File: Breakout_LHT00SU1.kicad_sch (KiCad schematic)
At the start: 1 part, among them J1 Conn_02x10_Odd_Even

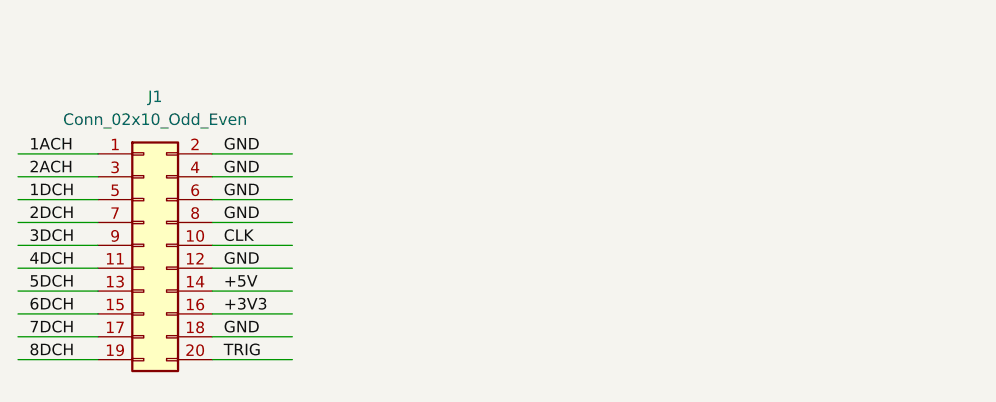
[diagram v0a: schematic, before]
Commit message: added 2x5 header + 2x BNC
output for digital signals and analog inputs
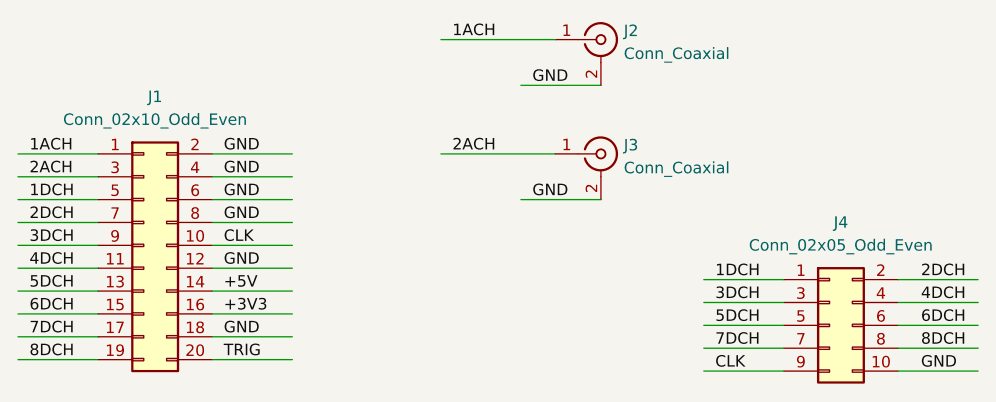
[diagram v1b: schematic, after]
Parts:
- added J2, J3: Conn_Coaxial, Connector_Coaxial:BNC_TEConnectivity_1478035_Horizontal, symbol Connector:Conn_Coaxial
- added J4: Conn_02x05_Odd_Even, Connector_PinHeader_2.54mm:PinHeader_2x05_P2.54mm_Vertical, symbol Connector_Generic:Conn_02x05_Odd_Even
- J1: footprint (none) -> Connector_PinHeader_2.54mm:PinHeader_2x10_P2.54mm_Horizontal
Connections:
- net 1ACH: now also J2.1 (In)
- net 1DCH: now also J4.1 (Pin_1)
- net 2ACH: now also J3.1 (In)
- net 2DCH: now also J4.2 (Pin_2)
- net 3DCH: now also J4.3 (Pin_3)
- net 4DCH: now also J4.4 (Pin_4)
- net 5DCH: now also J4.5 (Pin_5)
- net 6DCH: now also J4.6 (Pin_6)
- net 7DCH: now also J4.7 (Pin_7)
- net 8DCH: now also J4.8 (Pin_8)
- net CLK: now also J4.9 (Pin_9)
- net GND: now also J2.2 (Ext), J3.2 (Ext), J4.10 (Pin_10)
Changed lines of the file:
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@@
 (kicad_sch (version 20211123) (generator eeschema)
   (paper "A4")
+  (wire (pts (xy 97.79 43.18) (xy 106.68 43.18))
+    (stroke (width 0) (type default) (color 0 0 0 0))
+  )
   (wire (pts (xy 41.91 53.34) (xy 50.8 53.34))
     (stroke (width 0) (type default) (color 0 0 0 0))
   )
+  (wire (pts (xy 97.79 55.88) (xy 106.68 55.88))
+    (stroke (width 0) (type default) (color 0 0 0 0))
+  )
   (wire (pts (xy 41.91 58.42) (xy 50.8 58.42))
     (stroke (width 0) (type default) (color 0 0 0 0))
@@
     (stroke (width 0) (type default) (color 0 0 0 0))
   )
+  (wire (pts (xy 118.11 72.39) (xy 127 72.39))
+    (stroke (width 0) (type default) (color 0 0 0 0))
+  )
+  (wire (pts (xy 139.7 74.93) (xy 148.59 74.93))
+    (stroke (width 0) (type default) (color 0 0 0 0))
+  )
   (wire (pts (xy 63.5 53.34) (xy 72.39 53.34))
     (stroke (width 0) (type default) (color 0 0 0 0))
   )
+  (wire (pts (xy 139.7 72.39) (xy 148.59 72.39))
+    (stroke (width 0) (type default) (color 0 0 0 0))
+  )
+  (wire (pts (xy 118.11 67.31) (xy 127 67.31))
+    (stroke (width 0) (type default) (color 0 0 0 0))
+  )
   (wire (pts (xy 41.91 50.8) (xy 50.8 50.8))
     (stroke (width 0) (type default) (color 0 0 0 0))
   )
+  (wire (pts (xy 139.7 69.85) (xy 148.59 69.85))
+    (stroke (width 0) (type default) (color 0 0 0 0))
+  )
   (wire (pts (xy 41.91 71.12) (xy 50.8 71.12))
     (stroke (width 0) (type default) (color 0 0 0 0))
@@
     (stroke (width 0) (type default) (color 0 0 0 0))
   )
+  (wire (pts (xy 88.9 50.8) (xy 101.6 50.8))
+    (stroke (width 0) (type default) (color 0 0 0 0))
+  )
+  (wire (pts (xy 139.7 64.77) (xy 148.59 64.77))
+    (stroke (width 0) (type default) (color 0 0 0 0))
+  )
   (wire (pts (xy 41.91 73.66) (xy 50.8 73.66))
     (stroke (width 0) (type default) (color 0 0 0 0))
@@
     (stroke (width 0) (type default) (color 0 0 0 0))
   )
+  (wire (pts (xy 118.11 64.77) (xy 127 64.77))
+    (stroke (width 0) (type default) (color 0 0 0 0))
+  )
   (wire (pts (xy 63.5 71.12) (xy 72.39 71.12))
     (stroke (width 0) (type default) (color 0 0 0 0))
@@
     (stroke (width 0) (type default) (color 0 0 0 0))
   )
+  (wire (pts (xy 88.9 38.1) (xy 101.6 38.1))
+    (stroke (width 0) (type default) (color 0 0 0 0))
+  )
   (wire (pts (xy 63.5 66.04) (xy 72.39 66.04))
     (stroke (width 0) (type default) (color 0 0 0 0))
   )
+  (wire (pts (xy 118.11 69.85) (xy 127 69.85))
+    (stroke (width 0) (type default) (color 0 0 0 0))
+  )
   (wire (pts (xy 63.5 73.66) (xy 72.39 73.66))
     (stroke (width 0) (type default) (color 0 0 0 0))
   )
+  (wire (pts (xy 139.7 67.31) (xy 148.59 67.31))
+    (stroke (width 0) (type default) (color 0 0 0 0))
+  )
+  (wire (pts (xy 118.11 74.93) (xy 127 74.93))
+    (stroke (width 0) (type default) (color 0 0 0 0))
+  )
   (wire (pts (xy 41.91 66.04) (xy 50.8 66.04))
     (stroke (width 0) (type default) (color 0 0 0 0))
@@
     (effects (font (size 1.27 1.27)) (justify left bottom))
   )
+  (label "4DCH" (at 142.24 67.31 0)
+    (effects (font (size 1.27 1.27)) (justify left bottom))
+  )
   (label "3DCH" (at 43.18 60.96 0)
     (effects (font (size 1.27 1.27)) (justify left bottom))
   )
+  (label "2ACH" (at 90.17 50.8 0)
+    (effects (font (size 1.27 1.27)) (justify left bottom))
+  )
   (label "8DCH" (at 43.18 73.66 0)
     (effects (font (size 1.27 1.27)) (justify left bottom))
@@
     (effects (font (size 1.27 1.27)) (justify left bottom))
   )
+  (label "2DCH" (at 142.24 64.77 0)
+    (effects (font (size 1.27 1.27)) (justify left bottom))
+  )
+  (label "GND" (at 99.06 55.88 0)
+    (effects (font (size 1.27 1.27)) (justify left bottom))
+  )
+  (label "5DCH" (at 119.38 69.85 0)
+    (effects (font (size 1.27 1.27)) (justify left bottom))
+  )
   (label "CLK" (at 64.77 60.96 0)
     (effects (font (size 1.27 1.27)) (justify left bottom))
@@
     (effects (font (size 1.27 1.27)) (justify left bottom))
   )
+  (label "8DCH" (at 142.24 72.39 0)
+    (effects (font (size 1.27 1.27)) (justify left bottom))
+  )
+  (label "1ACH" (at 90.17 38.1 0)
+    (effects (font (size 1.27 1.27)) (justify left bottom))
+  )
+  (label "GND" (at 99.06 43.18 0)
+    (effects (font (size 1.27 1.27)) (justify left bottom))
+  )
   (label "2DCH" (at 43.18 58.42 0)
     (effects (font (size 1.27 1.27)) (justify left bottom))
@@
     (effects (font (size 1.27 1.27)) (justify left bottom))
   )
+  (label "7DCH" (at 119.38 72.39 0)
+    (effects (font (size 1.27 1.27)) (justify left bottom))
+  )
   (label "1DCH" (at 43.18 55.88 0)
     (effects (font (size 1.27 1.27)) (justify left bottom))
   )
+  (label "1DCH" (at 119.38 64.77 0)
+    (effects (font (size 1.27 1.27)) (justify left bottom))
+  )
+  (label "GND" (at 142.24 74.93 0)
+    (effects (font (size 1.27 1.27)) (justify left bottom))
+  )
   (label "GND" (at 64.77 50.8 0)
     (effects (font (size 1.27 1.27)) (justify left bottom))
   )
+  (label "CLK" (at 119.38 74.93 0)
+    (effects (font (size 1.27 1.27)) (justify left bottom))
+  )
+  (label "6DCH" (at 142.24 69.85 0)
+    (effects (font (size 1.27 1.27)) (justify left bottom))
+  )
   (label "GND" (at 64.77 63.5 0)
     (effects (font (size 1.27 1.27)) (justify left bottom))
@@
   )
   (label "1ACH" (at 43.18 50.8 0)
+    (effects (font (size 1.27 1.27)) (justify left bottom))
+  )
+  (label "3DCH" (at 119.38 67.31 0)
     (effects (font (size 1.27 1.27)) (justify left bottom))
   )
@@
     (property "Reference" "J1" (id 0) (at 57.15 44.45 0))
     (property "Value" "Conn_02x10_Odd_Even" (id 1) (at 57.15 46.99 0))
-    (property "Footprint" "" (id 2) (at 55.88 60.96 0)
+    (property "Footprint" "Connector_PinHeader_2.54mm:PinHeader_2x10_P2.54mm_Horizontal" (id 2) (at 55.88 60.96 0)
       (effects (font (size 1.27 1.27)) hide)
     )
@@
     (pin "9")
   )
+  (symbol (lib_id "Connector_Generic:Conn_02x05_Odd_Even") (at 132.08 69.85 0) (unit 1)
+    (in_bom yes) (on_board yes) (fields_autoplaced)
+    (property "Reference" "J4" (id 0) (at 133.35 58.42 0))
+    (property "Value" "Conn_02x05_Odd_Even" (id 1) (at 133.35 60.96 0))
+    (property "Footprint" "Connector_PinHeader_2.54mm:PinHeader_2x05_P2.54mm_Vertical" (id 2) (at 132.08 69.85 0)
+      (effects (font (size 1.27 1.27)) hide)
+    )
+    (property "Datasheet" "~" (id 3) (at 132.08 69.85 0)
+      (effects (font (size 1.27 1.27)) hide)
+    )
+    (pin "1")
+    (pin "10")
+    (pin "2")
+    (pin "3")
+    (pin "4")
+    (pin "5")
+    (pin "6")
+    (pin "7")
+    (pin "8")
+    (pin "9")
+  )
+  (symbol (lib_id "Connector:Conn_Coaxial") (at 106.68 50.8 0) (unit 1)
+    (in_bom yes) (on_board yes) (fields_autoplaced)
+    (property "Reference" "J3" (id 0) (at 109.22 49.8231 0)
+      (effects (font (size 1.27 1.27)) (justify left))
+    )
+    (property "Value" "Conn_Coaxial" (id 1) (at 109.22 52.3631 0)
+      (effects (font (size 1.27 1.27)) (justify left))
+    )
+    (property "Footprint" "Connector_Coaxial:BNC_TEConnectivity_1478035_Horizontal" (id 2) (at 106.68 50.8 0)
+      (effects (font (size 1.27 1.27)) hide)
+    )
+    (property "Datasheet" " ~" (id 3) (at 106.68 50.8 0)
+      (effects (font (size 1.27 1.27)) hide)
+    )
+    (pin "1")
+    (pin "2")
+  )
+  (symbol (lib_id "Connector:Conn_Coaxial") (at 106.68 38.1 0) (unit 1)
+    (in_bom yes) (on_board yes) (fields_autoplaced)
+    (property "Reference" "J2" (id 0) (at 109.22 37.1231 0)
+      (effects (font (size 1.27 1.27)) (justify left))
+    )
+    (property "Value" "Conn_Coaxial" (id 1) (at 109.22 39.6631 0)
+      (effects (font (size 1.27 1.27)) (justify left))
+    )
+    (property "Footprint" "Connector_Coaxial:BNC_TEConnectivity_1478035_Horizontal" (id 2) (at 106.68 38.1 0)
+      (effects (font (size 1.27 1.27)) hide)
+    )
+    (property "Datasheet" " ~" (id 3) (at 106.68 38.1 0)
+      (effects (font (size 1.27 1.27)) hide)
+    )
+    (pin "1")
+    (pin "2")
+  )
   (sheet_instances
     (path "/" (page "1"))
@@
   (symbol_instances
     (path "/1550fba1-bf41-49b6-a309-e7cbe1c7a73a"
-      (reference "J1") (unit 1) (value "Conn_02x10_Odd_Even") (footprint "")
-    )
-  )
+      (reference "J1") (unit 1) (value "Conn_02x10_Odd_Even") (footprint "Connector_PinHeader_2.54mm:PinHeader_2x10_P2.54mm_Horizontal")
+    )
+    (path "/b47147e5-09a2-4c5d-9526-11886fb6c153"
+      (reference "J2") (unit 1) (value "Conn_Coaxial") (footprint "Connector_Coaxial:BNC_TEConnectivity_1478035_Horizontal")
+    )
+    (path "/9e8790fe-99a4-4b12-ba62-e6be7ea4608a"
+      (reference "J3") (unit 1) (value "Conn_Coaxial") (footprint "Connector_Coaxial:BNC_TEConnectivity_1478035_Horizontal")
+    )
+    (path "/70fc3487-7898-458b-9d17-087925933edb"
+      (reference "J4") (unit 1) (value "Conn_02x05_Odd_Even") (footprint "Connector_PinHeader_2.54mm:PinHeader_2x05_P2.54mm_Vertical")
+    )
+  )

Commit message: updated layout (first iteration done)
done with first iteration, needs some improvements in order to save PCB space...
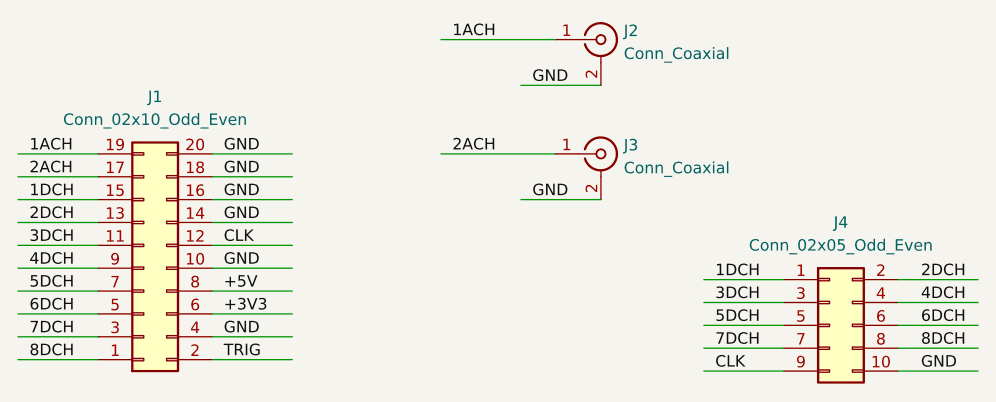
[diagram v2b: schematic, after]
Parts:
- J4: footprint Connector_PinHeader_2.54mm:PinHeader_2x05_P2.54mm_Vertical -> Connector_PinHeader_2.54mm:PinHeader_2x05_P2.54mm_Horizontal
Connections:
- net +3V3: now also J1.6 (Pin_6); no longer J1.16 (Pin_16)
- net +5V: now also J1.8 (Pin_8); no longer J1.14 (Pin_14)
- net 1ACH: now also J1.19 (Pin_19); no longer J1.1 (Pin_1)
- net 1DCH: now also J1.15 (Pin_15); no longer J1.5 (Pin_5)
- net 2ACH: now also J1.17 (Pin_17); no longer J1.3 (Pin_3)
- net 2DCH: now also J1.13 (Pin_13); no longer J1.7 (Pin_7)
- net 3DCH: now also J1.11 (Pin_11); no longer J1.9 (Pin_9)
- net 4DCH: now also J1.9 (Pin_9); no longer J1.11 (Pin_11)
- net 5DCH: now also J1.7 (Pin_7); no longer J1.13 (Pin_13)
- net 6DCH: now also J1.5 (Pin_5); no longer J1.15 (Pin_15)
- net 7DCH: now also J1.3 (Pin_3); no longer J1.17 (Pin_17)
- net 8DCH: now also J1.1 (Pin_1); no longer J1.19 (Pin_19)
- net CLK: now also J1.12 (Pin_12); no longer J1.10 (Pin_10)
- net GND: now also J1.10 (Pin_10), J1.14 (Pin_14), J1.16 (Pin_16), J1.20 (Pin_20); no longer J1.12 (Pin_12), J1.2 (Pin_2), J1.6 (Pin_6), J1.8 (Pin_8)
- net TRIG: now also J1.2 (Pin_2); no longer J1.20 (Pin_20)
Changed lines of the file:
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@@
     (effects (font (size 1.27 1.27)) (justify left bottom))
   )
-  (symbol (lib_id "Connector_Generic:Conn_02x10_Odd_Even") (at 55.88 60.96 0) (unit 1)
+  (symbol (lib_id "Connector_Generic:Conn_02x10_Odd_Even") (at 55.88 63.5 0) (mirror x) (unit 1)
     (in_bom yes) (on_board yes) (fields_autoplaced)
     (property "Reference" "J1" (id 0) (at 57.15 44.45 0))
     (property "Value" "Conn_02x10_Odd_Even" (id 1) (at 57.15 46.99 0))
-    (property "Footprint" "Connector_PinHeader_2.54mm:PinHeader_2x10_P2.54mm_Horizontal" (id 2) (at 55.88 60.96 0)
+    (property "Footprint" "Connector_PinHeader_2.54mm:PinHeader_2x10_P2.54mm_Horizontal" (id 2) (at 55.88 63.5 0)
       (effects (font (size 1.27 1.27)) hide)
     )
-    (property "Datasheet" "~" (id 3) (at 55.88 60.96 0)
+    (property "Datasheet" "~" (id 3) (at 55.88 63.5 0)
       (effects (font (size 1.27 1.27)) hide)
     )
@@
     (property "Reference" "J4" (id 0) (at 133.35 58.42 0))
     (property "Value" "Conn_02x05_Odd_Even" (id 1) (at 133.35 60.96 0))
-    (property "Footprint" "Connector_PinHeader_2.54mm:PinHeader_2x05_P2.54mm_Vertical" (id 2) (at 132.08 69.85 0)
+    (property "Footprint" "Connector_PinHeader_2.54mm:PinHeader_2x05_P2.54mm_Horizontal" (id 2) (at 132.08 69.85 0)
       (effects (font (size 1.27 1.27)) hide)
     )
@@
     )
     (path "/70fc3487-7898-458b-9d17-087925933edb"
-      (reference "J4") (unit 1) (value "Conn_02x05_Odd_Even") (footprint "Connector_PinHeader_2.54mm:PinHeader_2x05_P2.54mm_Vertical")
+      (reference "J4") (unit 1) (value "Conn_02x05_Odd_Even") (footprint "Connector_PinHeader_2.54mm:PinHeader_2x05_P2.54mm_Horizontal")
     )
   )
